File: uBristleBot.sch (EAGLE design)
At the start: 36 parts, among them M1 MOTOR-304-103, M2 MOTOR-304-103, Q1 2N7002BKV, U2 MCP7383X.DFN, U3 LM3668, U4 TPS727XX.DSE

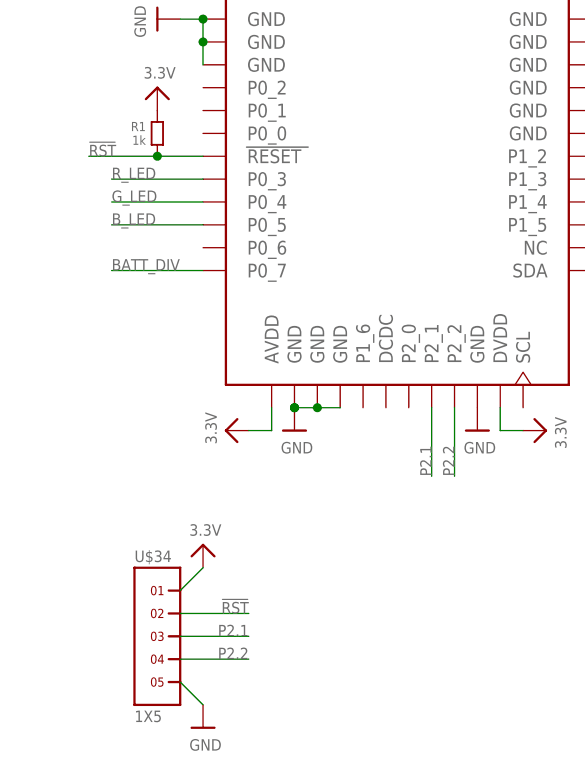
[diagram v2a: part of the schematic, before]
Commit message: Updated Inuctor and LED layer parts, and moved PWM pins. Ripped up programming connector in prep for Pogo Pins
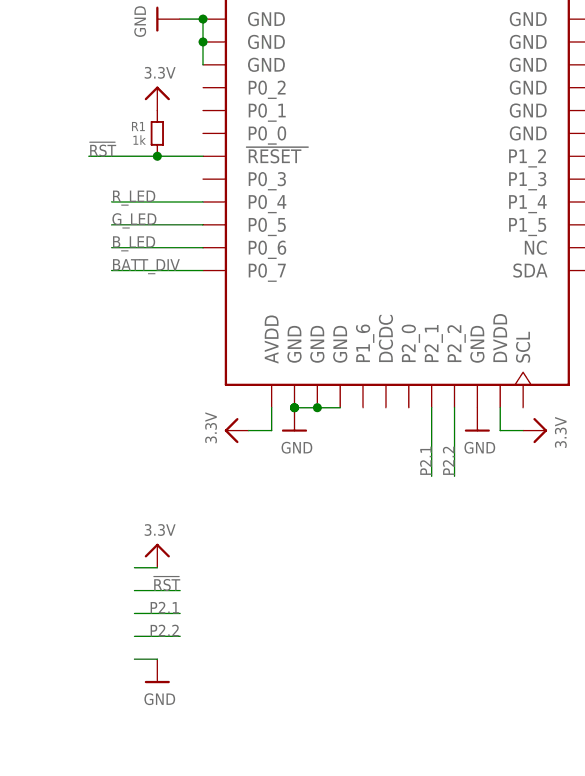
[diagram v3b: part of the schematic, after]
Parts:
- removed U$34: 1X5, headers(2mm):1X5
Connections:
- net !RST: no longer U$34.2
- net 3.3V: no longer U$34.1
- net B_LED: now also U1.P0_6; no longer U1.P0_5
- net GND: no longer U$34.5
- net G_LED: now also U1.P0_5; no longer U1.P0_4
- net P2.1: no longer U$34.3
- net P2.2: no longer U$34.4
- net R_LED: now also U1.P0_4; no longer U1.P0_3
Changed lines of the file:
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@@
 <grid distance="0.1" unitdist="inch" unit="inch" style="lines" multiple="1" display="no" altdistance="0.01" altunitdist="inch" altunit="inch"/>
 <layers>
-<layer number="1" name="Top" color="4" fill="1" visible="yes" active="no"/>
-<layer number="16" name="Bottom" color="1" fill="1" visible="yes" active="no"/>
-<layer number="17" name="Pads" color="2" fill="1" visible="yes" active="no"/>
-<layer number="18" name="Vias" color="2" fill="1" visible="yes" active="no"/>
-<layer number="19" name="Unrouted" color="6" fill="1" visible="yes" active="no"/>
-<layer number="20" name="Dimension" color="15" fill="1" visible="yes" active="no"/>
-<layer number="21" name="tPlace" color="7" fill="1" visible="yes" active="no"/>
-<layer number="22" name="bPlace" color="7" fill="1" visible="yes" active="no"/>
-<layer number="23" name="tOrigins" color="15" fill="1" visible="yes" active="no"/>
-<layer number="24" name="bOrigins" color="15" fill="1" visible="yes" active="no"/>
-<layer number="25" name="tNames" color="7" fill="1" visible="yes" active="no"/>
-<layer number="26" name="bNames" color="7" fill="1" visible="yes" active="no"/>
-<layer number="27" name="tValues" color="7" fill="1" visible="yes" active="no"/>
-<layer number="28" name="bValues" color="7" fill="1" visible="yes" active="no"/>
+<layer number="1" name="Top" color="4" fill="1" visible="no" active="no"/>
+<layer number="16" name="Bottom" color="1" fill="1" visible="no" active="no"/>
+<layer number="17" name="Pads" color="2" fill="1" visible="no" active="no"/>
+<layer number="18" name="Vias" color="2" fill="1" visible="no" active="no"/>
+<layer number="19" name="Unrouted" color="6" fill="1" visible="no" active="no"/>
+<layer number="20" name="Dimension" color="15" fill="1" visible="no" active="no"/>
+<layer number="21" name="tPlace" color="7" fill="1" visible="no" active="no"/>
+<layer number="22" name="bPlace" color="7" fill="1" visible="no" active="no"/>
+<layer number="23" name="tOrigins" color="15" fill="1" visible="no" active="no"/>
+<layer number="24" name="bOrigins" color="15" fill="1" visible="no" active="no"/>
+<layer number="25" name="tNames" color="7" fill="1" visible="no" active="no"/>
+<layer number="26" name="bNames" color="7" fill="1" visible="no" active="no"/>
+<layer number="27" name="tValues" color="7" fill="1" visible="no" active="no"/>
+<layer number="28" name="bValues" color="7" fill="1" visible="no" active="no"/>
 <layer number="29" name="tStop" color="7" fill="3" visible="no" active="no"/>
 <layer number="30" name="bStop" color="7" fill="6" visible="no" active="no"/>
@@
 <layer number="35" name="tGlue" color="7" fill="4" visible="no" active="no"/>
 <layer number="36" name="bGlue" color="7" fill="5" visible="no" active="no"/>
-<layer number="37" name="tTest" color="7" fill="1" visible="yes" active="no"/>
-<layer number="38" name="bTest" color="7" fill="1" visible="yes" active="no"/>
+<layer number="37" name="tTest" color="7" fill="1" visible="no" active="no"/>
+<layer number="38" name="bTest" color="7" fill="1" visible="no" active="no"/>
 <layer number="39" name="tKeepout" color="4" fill="11" visible="no" active="no"/>
 <layer number="40" name="bKeepout" color="1" fill="11" visible="no" active="no"/>
@@
 <layer number="44" name="Drills" color="7" fill="1" visible="no" active="no"/>
 <layer number="45" name="Holes" color="7" fill="1" visible="no" active="no"/>
-<layer number="46" name="Milling" color="3" fill="1" visible="yes" active="no"/>
-<layer number="47" name="Measures" color="7" fill="1" visible="yes" active="no"/>
-<layer number="48" name="Document" color="7" fill="1" visible="yes" active="no"/>
-<layer number="49" name="Reference" color="7" fill="1" visible="yes" active="no"/>
-<layer number="50" name="dxf" color="7" fill="1" visible="yes" active="no"/>
-<layer number="51" name="tDocu" color="7" fill="1" visible="yes" active="no"/>
-<layer number="52" name="bDocu" color="7" fill="1" visible="yes" active="no"/>
-<layer number="53" name="tGND_GNDA" color="7" fill="9" visible="yes" active="no"/>
-<layer number="54" name="bGND_GNDA" color="1" fill="9" visible="yes" active="no"/>
-<layer number="56" name="wert" color="7" fill="1" visible="yes" active="no"/>
-<layer number="59" name="Invisible" color="7" fill="1" visible="yes" active="no"/>
-<layer number="61" name="stand" color="7" fill="1" visible="yes" active="no"/>
+<layer number="46" name="Milling" color="3" fill="1" visible="no" active="no"/>
+<layer number="47" name="Measures" color="7" fill="1" visible="no" active="no"/>
+<layer number="48" name="Document" color="7" fill="1" visible="no" active="no"/>
+<layer number="49" name="Reference" color="7" fill="1" visible="no" active="no"/>
+<layer number="50" name="dxf" color="7" fill="1" visible="no" active="no"/>
+<layer number="51" name="tDocu" color="7" fill="1" visible="no" active="no"/>
+<layer number="52" name="bDocu" color="7" fill="1" visible="no" active="no"/>
+<layer number="53" name="tGND_GNDA" color="7" fill="9" visible="no" active="no"/>
+<layer number="54" name="bGND_GNDA" color="1" fill="9" visible="no" active="no"/>
+<layer number="56" name="wert" color="7" fill="1" visible="no" active="no"/>
+<layer number="59" name="Invisible" color="7" fill="1" visible="no" active="no"/>
+<layer number="61" name="stand" color="7" fill="1" visible="no" active="no"/>
 <layer number="90" name="Modules" color="5" fill="1" visible="yes" active="yes"/>
 <layer number="91" name="Nets" color="2" fill="1" visible="yes" active="yes"/>
@@
 <part name="C8" library="standardparts" deviceset="CAPACITOR" device=".0402" value=".1uF"/>
 <part name="C9" library="standardparts" deviceset="CAPACITOR" device=".0402" value=".1uF"/>
-<part name="U$34" library="headers(2mm)" deviceset="1X5" device=""/>
 <part name="U$35" library="microbuilder" deviceset="GND" device=""/>
 <part name="U$36" library="microbuilder" deviceset="3.3V" device=""/>
@@
 <instance part="C8" gate="G$1" x="187.96" y="71.12" rot="MR270"/>
 <instance part="C9" gate="G$1" x="226.06" y="71.12" rot="MR270"/>
-<instance part="U$34" gate="G$1" x="30.48" y="22.86"/>
-<instance part="U$35" gate="G$1" x="35.56" y="12.7"/>
-<instance part="U$36" gate="G$1" x="35.56" y="33.02"/>
+<instance part="U$35" gate="G$1" x="30.48" y="17.78"/>
+<instance part="U$36" gate="G$1" x="30.48" y="33.02"/>
 <instance part="C10" gate="G$1" x="116.84" y="66.04" rot="R270"/>
 <instance part="U$37" gate="G$1" x="38.1" y="45.72" rot="R90"/>
@@
 <segment>
 <pinref part="U$35" gate="G$1" pin="GND"/>
-<pinref part="U$34" gate="G$1" pin="5"/>
-<wire x1="35.56" y1="15.24" x2="33.02" y2="17.78" width="0.1524" layer="91"/>
+<wire x1="30.48" y1="20.32" x2="27.94" y2="20.32" width="0.1524" layer="91"/>
 </segment>
 <segment>
@@
 </segment>
 <segment>
-<pinref part="U1" gate="G$1" pin="P0_3"/>
-<wire x1="35.56" y1="73.66" x2="25.4" y2="73.66" width="0.1524" layer="91"/>
-<label x="25.4" y="73.66" size="1.27" layer="95"/>
+<pinref part="U1" gate="G$1" pin="P0_4"/>
+<wire x1="25.4" y1="71.12" x2="35.56" y2="71.12" width="0.1524" layer="91"/>
+<label x="25.4" y="71.12" size="1.27" layer="95"/>
 </segment>
 </net>
@@
 </segment>
 <segment>
-<pinref part="U1" gate="G$1" pin="P0_4"/>
-<wire x1="25.4" y1="71.12" x2="35.56" y2="71.12" width="0.1524" layer="91"/>
-<label x="25.4" y="71.12" size="1.27" layer="95"/>
+<pinref part="U1" gate="G$1" pin="P0_5"/>
+<wire x1="35.56" y1="68.58" x2="25.4" y2="68.58" width="0.1524" layer="91"/>
+<label x="25.4" y="68.58" size="1.27" layer="95"/>
 </segment>
 </net>
@@
 </segment>
 <segment>
-<pinref part="U1" gate="G$1" pin="P0_5"/>
-<wire x1="35.56" y1="68.58" x2="25.4" y2="68.58" width="0.1524" layer="91"/>
-<label x="25.4" y="68.58" size="1.27" layer="95"/>
+<pinref part="U1" gate="G$1" pin="P0_6"/>
+<wire x1="35.56" y1="66.04" x2="25.4" y2="66.04" width="0.1524" layer="91"/>
+<label x="25.4" y="66.04" size="1.27" layer="95"/>
 </segment>
 </net>
@@
 </segment>
 <segment>
-<pinref part="U$34" gate="G$1" pin="1"/>
 <pinref part="U$36" gate="G$1" pin="3.3V"/>
-<wire x1="33.02" y1="27.94" x2="35.56" y2="30.48" width="0.1524" layer="91"/>
+<wire x1="27.94" y1="30.48" x2="30.48" y2="30.48" width="0.1524" layer="91"/>
 </segment>
 <segment>
@@
 </segment>
 <segment>
-<pinref part="U$34" gate="G$1" pin="2"/>
-<wire x1="33.02" y1="25.4" x2="40.64" y2="25.4" width="0.1524" layer="91"/>
-<label x="40.64" y="25.4" size="1.27" layer="95" rot="MR0"/>
+<wire x1="27.94" y1="27.94" x2="33.02" y2="27.94" width="0.1524" layer="91"/>
+<label x="33.02" y="27.94" size="1.27" layer="95" rot="MR0"/>
 </segment>
 </net>
@@
 </segment>
 <segment>
-<pinref part="U$34" gate="G$1" pin="3"/>
-<wire x1="40.64" y1="22.86" x2="33.02" y2="22.86" width="0.1524" layer="91"/>
-<label x="40.64" y="22.86" size="1.27" layer="95" rot="MR0"/>
+<wire x1="33.02" y1="25.4" x2="27.94" y2="25.4" width="0.1524" layer="91"/>
+<label x="33.02" y="25.4" size="1.27" layer="95" rot="MR0"/>
 </segment>
 </net>
@@
 </segment>
 <segment>
-<pinref part="U$34" gate="G$1" pin="4"/>
-<wire x1="33.02" y1="20.32" x2="40.64" y2="20.32" width="0.1524" layer="91"/>
-<label x="40.64" y="20.32" size="1.27" layer="95" rot="MR0"/>
-</segment>
-</net>
+<wire x1="27.94" y1="22.86" x2="33.02" y2="22.86" width="0.1524" layer="91"/>
+<label x="33.02" y="22.86" size="1.27" layer="95" rot="MR0"/>
+</segment>
+</net>

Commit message: Finished layout of v0.2
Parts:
- added TP1, TP2, TP3, TP4, TP5: PCB_PAD.42MIL, mil_max:PCB_PAD.42MIL
- added U$34: 1X1, headers.edge(.1in):1X1
- U$31: value 1X2 -> 1X1; device headers(2mm):1X2 -> headers.edge(.1in):1X1
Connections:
- net !RST: now also TP2.PIN
- net 3.3V: now also TP1.PIN
- net GND: now also SW1.A, TP5.PIN, U$34.1; no longer SW1.B, U$31.2
- net P2.1: now also TP3.PIN
- net P2.2: now also TP4.PIN
- net VBAT: now also SW1.B; no longer SW1.A
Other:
- moved on the sheet: SW1
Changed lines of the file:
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@@
 <part name="U$30" library="microbuilder" deviceset="3.3V" device=""/>
 <part name="FRAME1" library="microbuilder" deviceset="FRAME_A4" device=""/>
-<part name="U$31" library="headers(2mm)" deviceset="1X2" device=""/>
 <part name="U$32" library="microbuilder" deviceset="VBAT" device=""/>
 <part name="U$33" library="microbuilder" deviceset="GND" device=""/>
@@
 <part name="C10" library="standardparts" deviceset="CAPACITOR" device=".0402" value=".1uF"/>
 <part name="U$37" library="microbuilder" deviceset="3.3V" device=""/>
+<part name="TP1" library="mil_max" deviceset="PCB_PAD" device=".42MIL"/>
+<part name="TP2" library="mil_max" deviceset="PCB_PAD" device=".42MIL"/>
+<part name="TP3" library="mil_max" deviceset="PCB_PAD" device=".42MIL"/>
+<part name="TP4" library="mil_max" deviceset="PCB_PAD" device=".42MIL"/>
+<part name="TP5" library="mil_max" deviceset="PCB_PAD" device=".42MIL"/>
+<part name="U$31" library="headers.edge(.1in)" deviceset="1X1" device=""/>
+<part name="U$34" library="headers.edge(.1in)" deviceset="1X1" device=""/>
 </parts>
 <sheets>
@@
 <instance part="M1" gate="G$1" x="190.5" y="71.12"/>
 <instance part="M2" gate="G$1" x="228.6" y="73.66" rot="MR180"/>
-<instance part="SW1" gate="G$1" x="190.5" y="134.62" rot="MR0"/>
+<instance part="SW1" gate="G$1" x="190.5" y="139.7" smashed="yes" rot="R180">
+<attribute name="NAME" x="189.23" y="137.16" size="1.016" layer="95" font="vector" rot="R90"/>
+<attribute name="VALUE" x="193.04" y="141.605" size="1.016" layer="96" font="vector" rot="R180"/>
+</instance>
 <instance part="USB2" gate="G$1" x="30.48" y="139.7"/>
 <instance part="U$1" gate="G$1" x="83.82" y="91.44" rot="R90"/>
@@
 <instance part="U$6" gate="G$1" x="142.24" y="144.78"/>
 <instance part="U$21" gate="G$1" x="190.5" y="142.24"/>
-<instance part="U$22" gate="G$1" x="190.5" y="132.08"/>
+<instance part="U$22" gate="G$1" x="190.5" y="134.62"/>
 <instance part="L1" gate="G$1" x="165.1" y="147.32"/>
 <instance part="U$23" gate="G$1" x="142.24" y="127"/>
@@
 <instance part="U$30" gate="G$1" x="81.28" y="58.42"/>
 <instance part="FRAME1" gate="G$1" x="0" y="0"/>
-<instance part="U$31" gate="G$1" x="114.3" y="134.62" smashed="yes">
-<attribute name="VALUE" x="111.76" y="127.635" size="1.27" layer="96" font="vector"/>
-</instance>
 <instance part="U$32" gate="G$1" x="119.38" y="139.7"/>
 <instance part="U$33" gate="G$1" x="119.38" y="127"/>
 <instance part="C8" gate="G$1" x="187.96" y="71.12" rot="MR270"/>
 <instance part="C9" gate="G$1" x="226.06" y="71.12" rot="MR270"/>
-<instance part="U$35" gate="G$1" x="30.48" y="17.78"/>
-<instance part="U$36" gate="G$1" x="30.48" y="33.02"/>
+<instance part="U$35" gate="G$1" x="17.78" y="17.78"/>
+<instance part="U$36" gate="G$1" x="17.78" y="33.02"/>
 <instance part="C10" gate="G$1" x="116.84" y="66.04" rot="R270"/>
 <instance part="U$37" gate="G$1" x="38.1" y="45.72" rot="R90"/>
+<instance part="TP1" gate="G$1" x="22.86" y="30.48"/>
+<instance part="TP2" gate="G$1" x="25.4" y="27.94" rot="MR0"/>
+<instance part="TP3" gate="G$1" x="27.94" y="25.4" rot="MR0"/>
+<instance part="TP4" gate="G$1" x="30.48" y="22.86" rot="MR0"/>
+<instance part="TP5" gate="G$1" x="33.02" y="20.32" rot="MR0"/>
+<instance part="U$31" gate="G$1" x="114.3" y="137.16" smashed="yes"/>
+<instance part="U$34" gate="G$1" x="114.3" y="129.54" smashed="yes"/>
 </instances>
 <busses>
@@
 </segment>
 <segment>
-<pinref part="SW1" gate="G$1" pin="B"/>
-<pinref part="U$22" gate="G$1" pin="GND"/>
-</segment>
-<segment>
 <pinref part="U$23" gate="G$1" pin="GND"/>
 <pinref part="C3" gate="G$1" pin="2"/>
@@
 </segment>
 <segment>
-<pinref part="U$31" gate="G$1" pin="2"/>
-<wire x1="116.84" y1="132.08" x2="119.38" y2="132.08" width="0.1524" layer="91"/>
-<pinref part="U$33" gate="G$1" pin="GND"/>
-<wire x1="119.38" y1="132.08" x2="119.38" y2="129.54" width="0.1524" layer="91"/>
-</segment>
-<segment>
 <pinref part="U$35" gate="G$1" pin="GND"/>
-<wire x1="30.48" y1="20.32" x2="27.94" y2="20.32" width="0.1524" layer="91"/>
+<wire x1="17.78" y1="20.32" x2="33.02" y2="20.32" width="0.1524" layer="91"/>
+<pinref part="TP5" gate="G$1" pin="PIN"/>
 </segment>
 <segment>
@@
 <wire x1="111.76" y1="63.5" x2="116.84" y2="63.5" width="0.1524" layer="91"/>
 <junction x="116.84" y="63.5"/>
+</segment>
+<segment>
+<pinref part="U$34" gate="G$1" pin="1"/>
+<pinref part="U$33" gate="G$1" pin="GND"/>
+<wire x1="116.84" y1="129.54" x2="119.38" y2="129.54" width="0.1524" layer="91"/>
+</segment>
+<segment>
+<pinref part="SW1" gate="G$1" pin="A"/>
+<pinref part="U$22" gate="G$1" pin="GND"/>
 </segment>
 </net>
@@
 <segment>
 <pinref part="U$36" gate="G$1" pin="3.3V"/>
-<wire x1="27.94" y1="30.48" x2="30.48" y2="30.48" width="0.1524" layer="91"/>
+<wire x1="22.86" y1="30.48" x2="17.78" y2="30.48" width="0.1524" layer="91"/>
+<pinref part="TP1" gate="G$1" pin="PIN"/>
 </segment>
 <segment>
@@
 </segment>
 <segment>
-<wire x1="27.94" y1="27.94" x2="33.02" y2="27.94" width="0.1524" layer="91"/>
-<label x="33.02" y="27.94" size="1.27" layer="95" rot="MR0"/>
+<wire x1="25.4" y1="27.94" x2="17.78" y2="27.94" width="0.1524" layer="91"/>
+<label x="17.78" y="27.94" size="1.27" layer="95"/>
+<pinref part="TP2" gate="G$1" pin="PIN"/>
 </segment>
 </net>
@@
 <net name="N$6" class="0">
 <segment>
-<pinref part="M1" gate="G$1" pin="2"/>
-<wire x1="190.5" y1="71.12" x2="187.96" y2="68.58" width="0.1524" layer="91"/>
 <pinref part="Q1" gate=".1" pin="D"/>
 <wire x1="187.96" y1="68.58" x2="182.88" y2="68.58" width="0.1524" layer="91"/>
@@
 <junction x="182.88" y="68.58"/>
 <pinref part="C8" gate="G$1" pin="2"/>
+<pinref part="M1" gate="G$1" pin="2"/>
+<wire x1="190.5" y1="71.12" x2="187.96" y2="68.58" width="0.1524" layer="91"/>
 <junction x="187.96" y="68.58"/>
 </segment>
@@
 <net name="N$8" class="0">
 <segment>
-<pinref part="M2" gate="G$1" pin="1"/>
-<wire x1="228.6" y1="71.12" x2="226.06" y2="68.58" width="0.1524" layer="91"/>
 <pinref part="Q1" gate=".2" pin="D"/>
 <wire x1="226.06" y1="68.58" x2="220.98" y2="68.58" width="0.1524" layer="91"/>
@@
 <junction x="220.98" y="68.58"/>
 <pinref part="C9" gate="G$1" pin="2"/>
+<pinref part="M2" gate="G$1" pin="1"/>
+<wire x1="228.6" y1="71.12" x2="226.06" y2="68.58" width="0.1524" layer="91"/>
 <junction x="226.06" y="68.58"/>
 </segment>
@@
 <wire x1="88.9" y1="137.16" x2="88.9" y2="139.7" width="0.1524" layer="91"/>
 <junction x="88.9" y="137.16"/>
-</segment>
-<segment>
-<pinref part="SW1" gate="G$1" pin="A"/>
-<pinref part="U$21" gate="G$1" pin="VBAT"/>
-<wire x1="190.5" y1="137.16" x2="190.5" y2="139.7" width="0.1524" layer="91"/>
 </segment>
 <segment>
@@
 </segment>
 <segment>
+<pinref part="U$32" gate="G$1" pin="VBAT"/>
 <pinref part="U$31" gate="G$1" pin="1"/>
-<wire x1="116.84" y1="134.62" x2="119.38" y2="134.62" width="0.1524" layer="91"/>
-<pinref part="U$32" gate="G$1" pin="VBAT"/>
-<wire x1="119.38" y1="134.62" x2="119.38" y2="137.16" width="0.1524" layer="91"/>
+<wire x1="116.84" y1="137.16" x2="119.38" y2="137.16" width="0.1524" layer="91"/>
+</segment>
+<segment>
+<pinref part="U$21" gate="G$1" pin="VBAT"/>
+<pinref part="SW1" gate="G$1" pin="B"/>
 </segment>
 </net>
@@
 <net name="VMOTOR" class="0">
 <segment>
-<pinref part="M1" gate="G$1" pin="1"/>
-<wire x1="190.5" y1="73.66" x2="187.96" y2="73.66" width="0.1524" layer="91"/>
 <pinref part="U$25" gate="G$1" pin="VMOTOR"/>
 <wire x1="187.96" y1="73.66" x2="182.88" y2="76.2" width="0.1524" layer="91"/>
@@
 <junction x="182.88" y="76.2"/>
 <pinref part="C8" gate="G$1" pin="1"/>
+<pinref part="M1" gate="G$1" pin="1"/>
+<wire x1="190.5" y1="73.66" x2="187.96" y2="73.66" width="0.1524" layer="91"/>
 <junction x="187.96" y="73.66"/>
 </segment>
 <segment>
-<pinref part="M2" gate="G$1" pin="2"/>
-<wire x1="228.6" y1="73.66" x2="226.06" y2="73.66" width="0.1524" layer="91"/>
 <pinref part="U$26" gate="G$1" pin="VMOTOR"/>
 <wire x1="226.06" y1="73.66" x2="220.98" y2="76.2" width="0.1524" layer="91"/>
@@
 <junction x="220.98" y="76.2"/>
 <pinref part="C9" gate="G$1" pin="1"/>
+<pinref part="M2" gate="G$1" pin="2"/>
+<wire x1="228.6" y1="73.66" x2="226.06" y2="73.66" width="0.1524" layer="91"/>
 <junction x="226.06" y="73.66"/>
 </segment>
@@
 </segment>
 <segment>
-<wire x1="33.02" y1="25.4" x2="27.94" y2="25.4" width="0.1524" layer="91"/>
-<label x="33.02" y="25.4" size="1.27" layer="95" rot="MR0"/>
+<wire x1="17.78" y1="25.4" x2="27.94" y2="25.4" width="0.1524" layer="91"/>
+<label x="17.78" y="25.4" size="1.27" layer="95"/>
+<pinref part="TP3" gate="G$1" pin="PIN"/>
 </segment>
 </net>
@@
 </segment>
 <segment>
-<wire x1="27.94" y1="22.86" x2="33.02" y2="22.86" width="0.1524" layer="91"/>
-<label x="33.02" y="22.86" size="1.27" layer="95" rot="MR0"/>
-</segment>
-</net>
+<wire x1="30.48" y1="22.86" x2="17.78" y2="22.86" width="0.1524" layer="91"/>
+<label x="17.78" y="22.86" size="1.27" layer="95"/>
+<pinref part="TP4" gate="G$1" pin="PIN"/>
+</segment>
+</net>
